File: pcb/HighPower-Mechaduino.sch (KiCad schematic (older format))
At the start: 31 parts, among them J1 SUPPLY, J2 STEPPER, P1 SWD, Q1 SSM3J328R, Q2 BSS138, SW1 SW_PUSH, U1 AS5047D, U2 AP2112K-3.3TRG1, U3 AT24CS64-SSHM

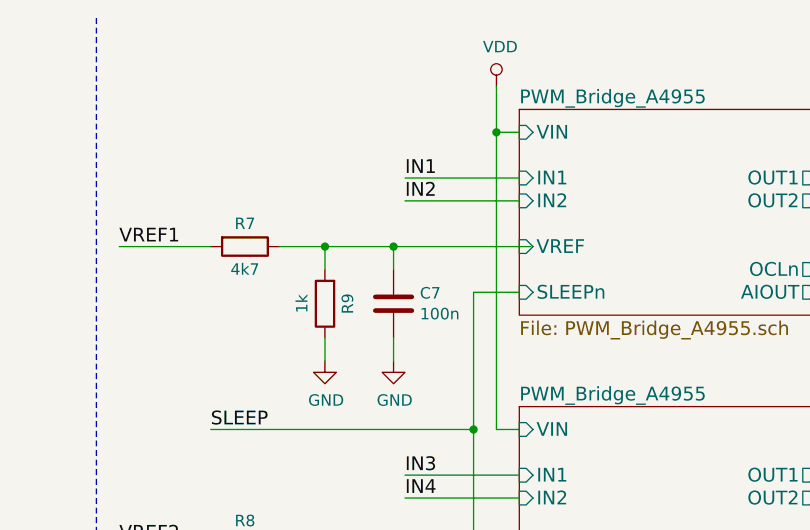
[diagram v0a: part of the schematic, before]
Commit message: Fix some assignment problems because of wrong library/component names
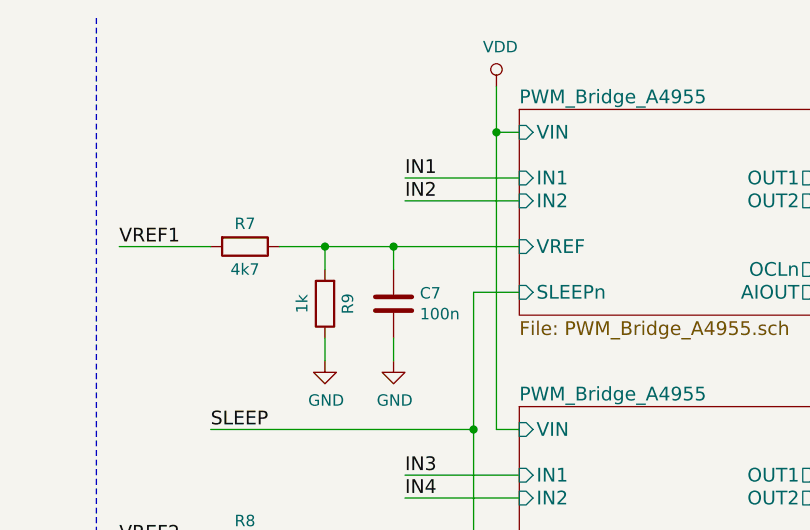
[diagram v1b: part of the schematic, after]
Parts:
- J1: footprint Terminal_Blocks:TerminalBlock_Pheonix_MPT-2.54mm_2pol -> Connectors_Terminal_Blocks:TerminalBlock_Pheonix_MPT-2.54mm_2pol
- J2: footprint Terminal_Blocks:TerminalBlock_Pheonix_MPT-2.54mm_4pol -> Connectors_Terminal_Blocks:TerminalBlock_Pheonix_MPT-2.54mm_4pol
- U1: footprint SSOP_Packages:TSSOP-14_4.4x5mm_Pitch0.65mm -> Housings_SSOP:TSSOP-14_4.4x5mm_Pitch0.65mm
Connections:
- net PWM_Bridge_A4955/OUT1 is gone; now on net PWM_Bridge_A4955/OUT1: J2.3
- net PWM_Bridge_A4955/OUT2 is gone; now on net PWM_Bridge_A4955/OUT2: J2.4
- net PWM_Bridge_A4955/VREF is gone; now on net PWM_Bridge_A4955/VREF: C8.2, R10.2, R8.1
- net PWM_Bridge_A4955/OUT1: no longer J2.1
- net PWM_Bridge_A4955/OUT2: no longer J2.2
- net PWM_Bridge_A4955/VREF: now reaches C7.2, R7.1, R9.2
- new net PWM_Bridge_A4955/OUT1: J2.1
- new net PWM_Bridge_A4955/OUT2: J2.2
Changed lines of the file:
@@
 F 0 "U1" H 3400 2600 50  0000 C CNN
 F 1 "AS5047D" H 4100 1600 50  0000 C CNN
-F 2 "SSOP_Packages:TSSOP-14_4.4x5mm_Pitch0.65mm" H 3800 1350 50  0001 C CNN
+F 2 "Housings_SSOP:TSSOP-14_4.4x5mm_Pitch0.65mm" H 3800 1350 50  0001 C CNN
 F 3 "" H 1650 3700 50  0000 C CNN
 	1    3800 2100
@@
 	7750 2800 8800 2800
 Wire Wire Line
-	7750 1500 8850 1500
-Wire Wire Line
 	7450 1500 7050 1500
 Wire Wire Line
@@
 	-1   0    0    1
 $EndComp
-Wire Wire Line
-	8250 1600 8250 1500
-Connection ~ 8250 1500
 $Comp
 L C C8
@@
 F 0 "J2" H 11131 2542 50  0000 C CNN
 F 1 "STEPPER" H 11131 2451 50  0000 C CNN
-F 2 "Terminal_Blocks:TerminalBlock_Pheonix_MPT-2.54mm_4pol" H 11050 1575 50  0001 C CNN
+F 2 "Connectors_Terminal_Blocks:TerminalBlock_Pheonix_MPT-2.54mm_4pol" H 11050 1575 50  0001 C CNN
 F 3 "" H 11025 2200 50  0001 C CNN
 	1    11050 2000
@@
 $EndComp
 Wire Wire Line
-	7950 1600 7950 1500
-Connection ~ 7950 1500
-Wire Wire Line
 	7950 1900 7950 2000
 $Comp
@@
 F 0 "J1" H 980 4892 50  0000 C CNN
 F 1 "SUPPLY" H 980 4801 50  0000 C CNN
-F 2 "Terminal_Blocks:TerminalBlock_Pheonix_MPT-2.54mm_2pol" H 900 4325 50  0001 C CNN
+F 2 "Connectors_Terminal_Blocks:TerminalBlock_Pheonix_MPT-2.54mm_2pol" H 900 4325 50  0001 C CNN
 F 3 "" H 875 4550 50  0001 C CNN
 	1    900  4550
@@
 	1    0    0    1
 $EndComp
+Wire Wire Line
+	7750 1500 8800 1500
+Wire Wire Line
+	8250 1600 8250 1500
+Connection ~ 8250 1500
+Wire Wire Line
+	7950 1600 7950 1500
+Connection ~ 7950 1500
 $EndSCHEMATC

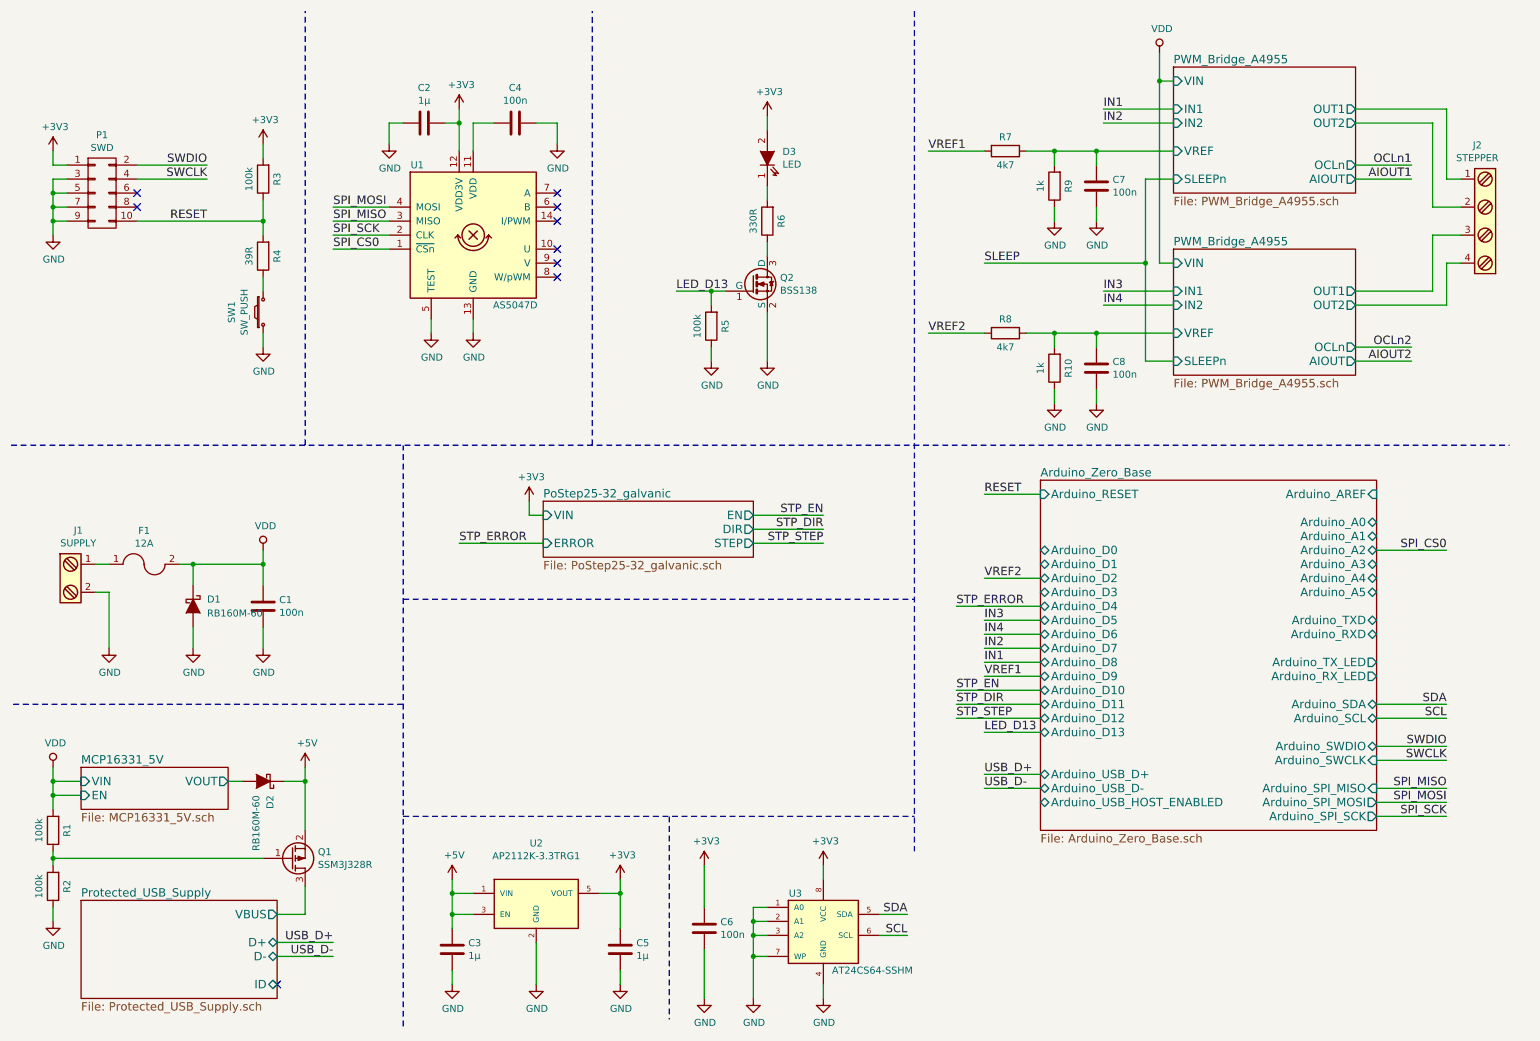
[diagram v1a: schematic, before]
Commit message: Place some components onto the PCB
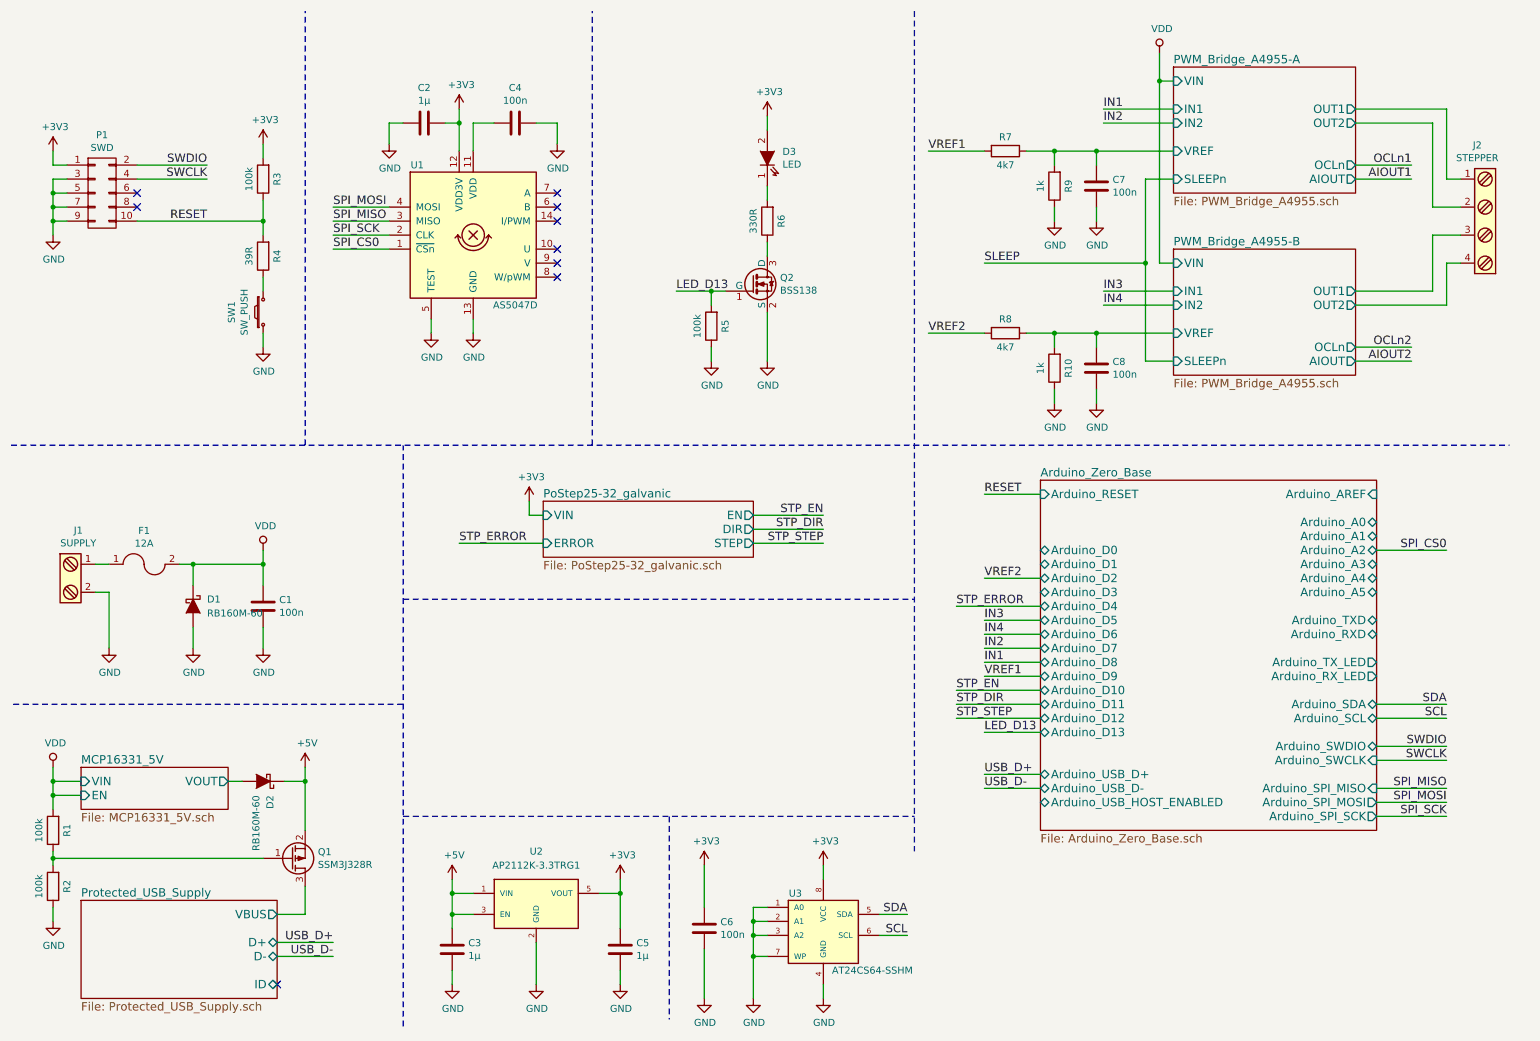
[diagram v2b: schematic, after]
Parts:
- U2: footprint Housings_SSOP:TSSOP-14_4.4x5mm_Pitch0.65mm -> TO_SOT_Packages_SMD:SOT-23-5
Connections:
- net PWM_Bridge_A4955/OUT1 renamed PWM_Bridge_A4955-A/OUT1
- net PWM_Bridge_A4955/OUT1 renamed PWM_Bridge_A4955-B/OUT1
- net PWM_Bridge_A4955/OUT2 renamed PWM_Bridge_A4955-A/OUT2
- net PWM_Bridge_A4955/OUT2 renamed PWM_Bridge_A4955-B/OUT2
- net PWM_Bridge_A4955/VREF renamed PWM_Bridge_A4955-A/VREF
- net PWM_Bridge_A4955/VREF renamed PWM_Bridge_A4955-B/VREF
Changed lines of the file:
@@
 S 8800 900  1300 900
 U 58077727
-F0 "PWM_Bridge_A4955" 60
+F0 "PWM_Bridge_A4955-A" 60
 F1 "PWM_Bridge_A4955.sch" 60
 F2 "VIN" I L 8800 1000 60
@@
 S 8800 2200 1300 900
 U 58084D17
-F0 "PWM_Bridge_A4955" 60
+F0 "PWM_Bridge_A4955-B" 60
 F1 "PWM_Bridge_A4955.sch" 60
 F2 "VIN" I L 8800 2300 60
@@
 U 1 1 58093871
 P 4250 6850
-F 0 "U2" H 4250 7258 50  0000 C CNN
-F 1 "AP2112K-3.3TRG1" H 4250 7167 50  0000 C CNN
-F 2 "Housings_SSOP:TSSOP-14_4.4x5mm_Pitch0.65mm" H 4250 7076 50  0001 C CIN
+F 0 "U2" H 4250 7200 50  0000 C CNN
+F 1 "AP2112K-3.3TRG1" H 4250 7100 50  0000 C CNN
+F 2 "TO_SOT_Packages_SMD:SOT-23-5" H 4250 7076 50  0001 C CIN
 F 3 "" H 4250 6850 50  0000 C CNN
 	1    4250 6850

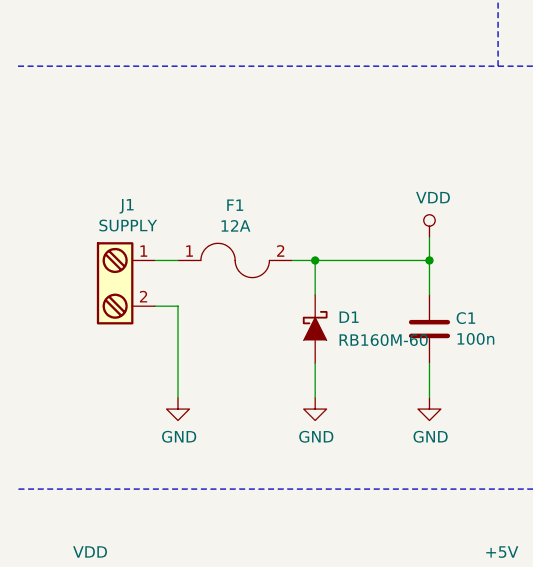
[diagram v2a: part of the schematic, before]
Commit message: Improve driver part of PCB I think I improved the Driver part of the PCB quit a bit by rearanging all of the components. But there are still many points which have to be worked on. This is still only a routing test. Later I will create usefull copper lines and adding copper zones for all high current lines.
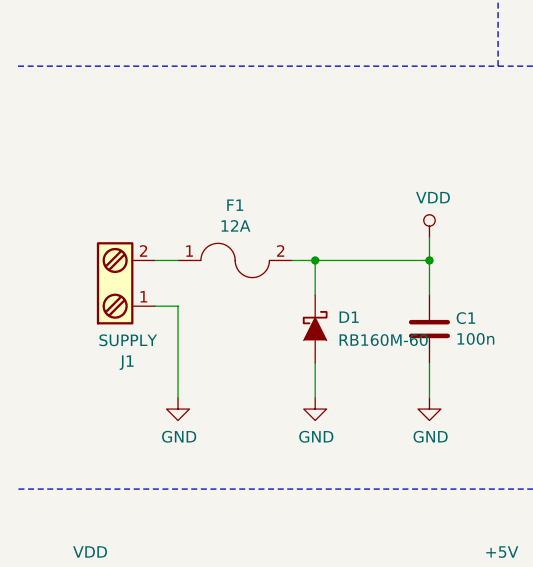
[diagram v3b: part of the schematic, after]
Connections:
- net GND: now also J1.1; no longer J1.2
- net at F1.1: now also J1.2; no longer J1.1
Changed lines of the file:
@@
 F 3 "" H 875 4550 50  0001 C CNN
 	1    900  4550
-	1    0    0    -1
+	1    0    0    1
 $EndComp
 $Comp
